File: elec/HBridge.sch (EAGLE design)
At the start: 22 parts, among them IC1 TL082P, IC2 TL082P, IC3 TL082P, T1 QSD124N

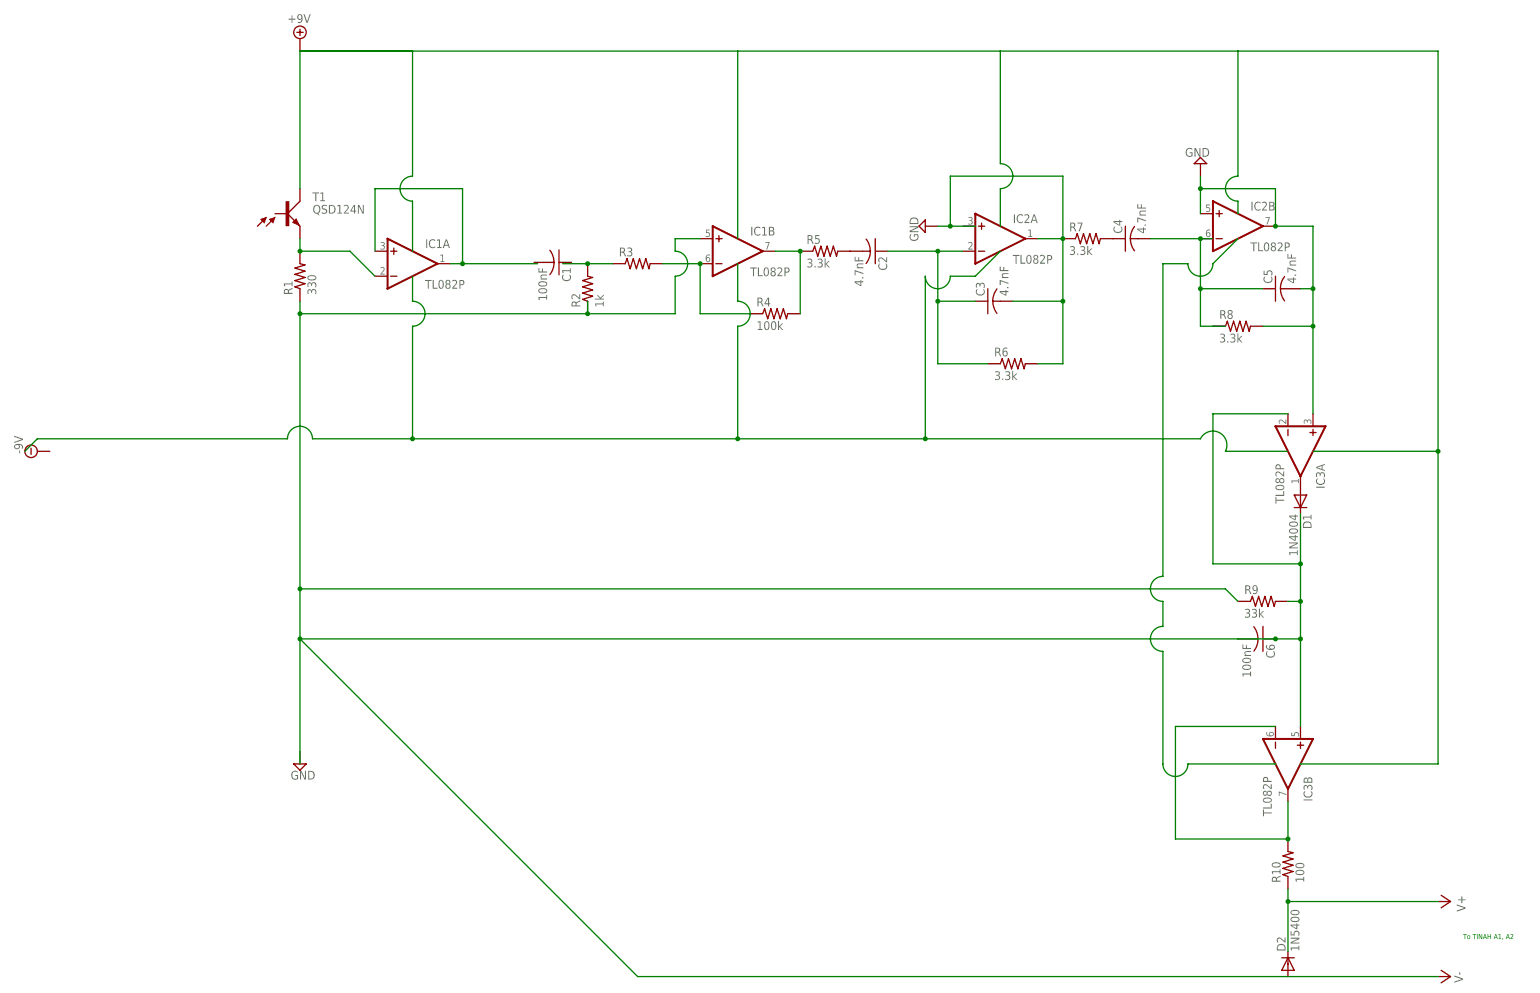
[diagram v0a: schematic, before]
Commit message: Hbridge and IR Detector circuits modified version June 13
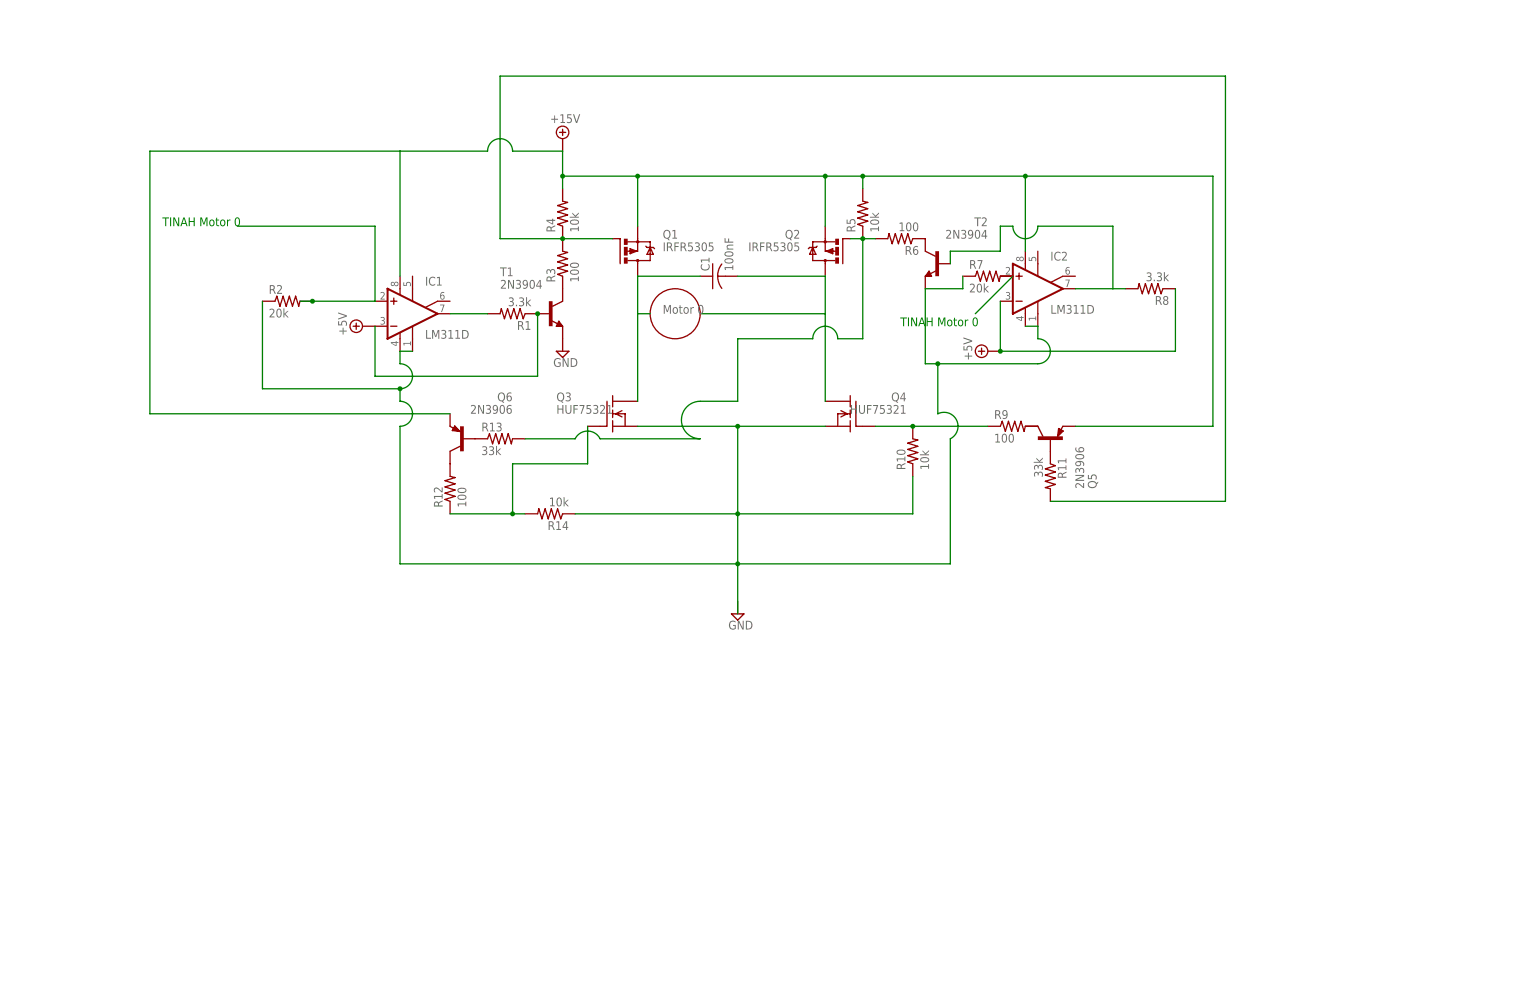
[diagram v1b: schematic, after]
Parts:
- removed C2: 4.7nF, resistor:C-US025-025X050
- removed C3: 4.7nF, resistor:C-US050-055X075
- removed C4: 4.7nF, resistor:C-US225-087X268
- removed C5: 4.7nF, resistor:C-US050-045X075
- removed C6: 100nF, resistor:C-US025-060X050
- removed D1: 1N4004, diode:1N4004
- removed D2: 1N5400, diode:1N5400
- removed IC3: TL082P, linear:TL082P
- added Q1, Q2: IRFR5305, transistor-power:IRFR5305
- added Q3, Q4: HUF75321, transistor-fet:FDS5680
- added Q5, Q6: 2N3906, transistor-pnp:2N3906
- added R11, R13: 33k, resistor:R-US_0204/2V
- added R12: 100, resistor:R-US_0204/2V
- added R14: 10k, resistor:R-US_0204/2V
- added T2: 2N3904, transistor:2N3904
- IC1, IC2: value TL082P -> LM311D; device linear:TL082P -> linear:LM311D
- R1: value 330 -> 3.3k; device resistor:R-US_0204/5 -> resistor:R-US_0204/2V
- R10: value 100 -> 10k; device resistor:R-US_0414/5V -> resistor:R-US_0204/2V
- R2: value 1k -> 20k; device resistor:R-US_0204/5 -> resistor:R-US_0204/2V
- R3: value (none) -> 100; device resistor:R-US_0207/5V -> resistor:R-US_0204/2V
- R4: value 100k -> 10k; device resistor:R-US_01005 -> resistor:R-US_0204/2V
- R5: value 3.3k -> 10k; device resistor:R-US_01005 -> resistor:R-US_0204/2V
- R6: value 3.3k -> 100; device resistor:R-US_0207/5V -> resistor:R-US_0204/2V
- R7: value 3.3k -> 20k; device resistor:R-US_0207/5V -> resistor:R-US_0204/2V
- R8: device resistor:R-US_0309/12 -> resistor:R-US_0204/2V
- R9: value 33k -> 100; device resistor:R-US_0207/5V -> resistor:R-US_0204/2V
- T1: value QSD124N -> 2N3904; device opto-trans-siemens:BP103 -> transistor:2N3904
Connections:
- removed net V+: D2.C, R10.1
- removed net V-: C6.1, C6.2, D1.C, D2.A, IC1B.+IN, IC3A.-IN, IC3B.+IN, R1.1, R2.1, R9.1, R9.2
- new net +5V: IC1.-IN, IC2.-IN, R1.1, R8.1, T1.B
- new net N$10: R7.2
- new net N$11: IC2.OUT, R8.2, T2.B
- new net N$15: Q6.B, R13.1
- new net N$16: Q3.G, R12.1, R14.2
- new net N$3: R3.1, T1.C
- net +15V: now also IC1.V+, IC2.V+, Q1.S, Q2.S, Q5.E, Q6.E, R4.2, R5.2; no longer T1.C
- net GND: now also T1.E; no longer C3.2, C5.2, IC2A.OUT, IC2B.+IN, IC2B.OUT, IC3A.+IN, R6.2, R7.1, R8.2
- net N$1: now also IC1.OUT; no longer IC1A.-IN, T1.E
- net N$12: now also Q1.G, R11.2, R3.2, R4.1; no longer IC3B.-IN, IC3B.OUT, R10.2
- net N$13: now also Q5.B, R11.1; no longer C4.1, R7.2
- net N$14: now also Q6.C, R12.2; no longer C4.2, C5.1, IC2B.-IN, R8.1
- net N$2: now also IC1.+IN, R2.2; no longer IC1A.+IN, IC1A.OUT
- net N$4: now also Q2.G, R13.2, R5.1, R6.2; no longer IC1B.-IN, R3.2, R4.1
- net N$5: now also IC1.GND, IC1.V-, IC2.GND, IC2.V-, Q3.S, Q4.S, R10.1, R14.1, R2.1, R7.1, T2.E; no longer IC1B.OUT, R4.2, R5.1
- net N$6: now also C1.2, Q2.D, Q4.D; no longer R2.2, R3.1
- net N$7: now also C1.1, Q1.D, Q3.D; no longer C2.1, C3.1, IC2A.-IN, R6.1
- net N$8: now also R6.1, T2.C; no longer C2.2, R5.2
- net N$9: now also Q4.G, R10.2, R9.1; no longer D1.A, IC3A.OUT
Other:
- note added: "Motor 0"
- note added: "TINAH Motor 0"
- note removed: "To TINAH A1, A2"
- moved on the sheet: C1, R1, R10, R2, R3, R4, R5, R6, R7, R8, R9

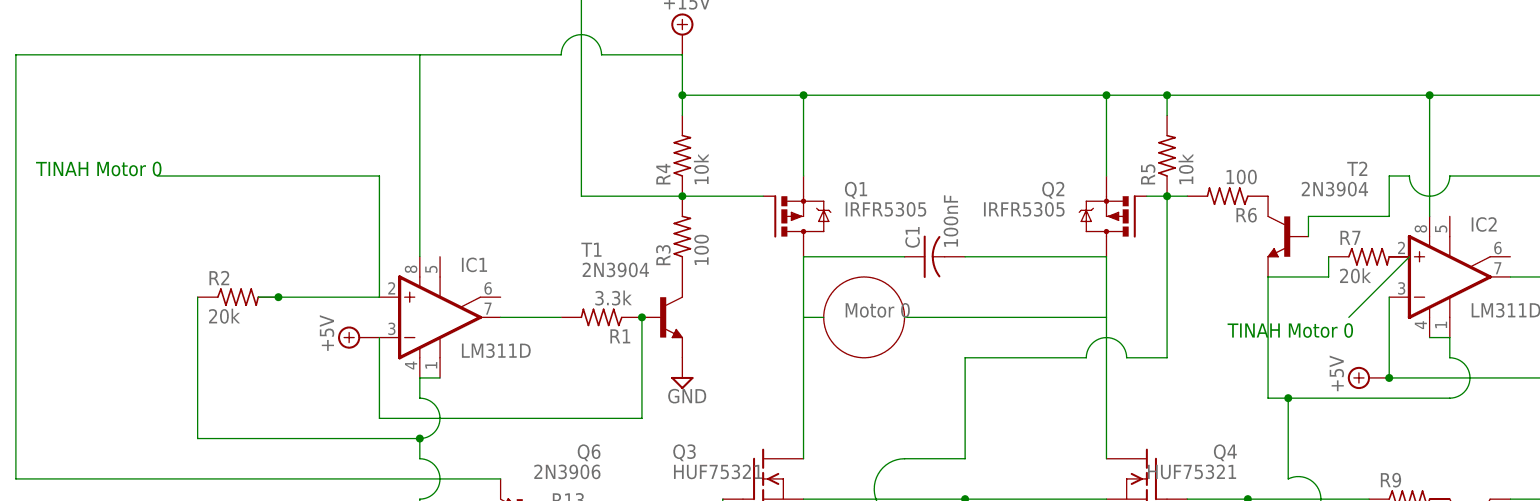
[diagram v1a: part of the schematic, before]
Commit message: Updated H bridge
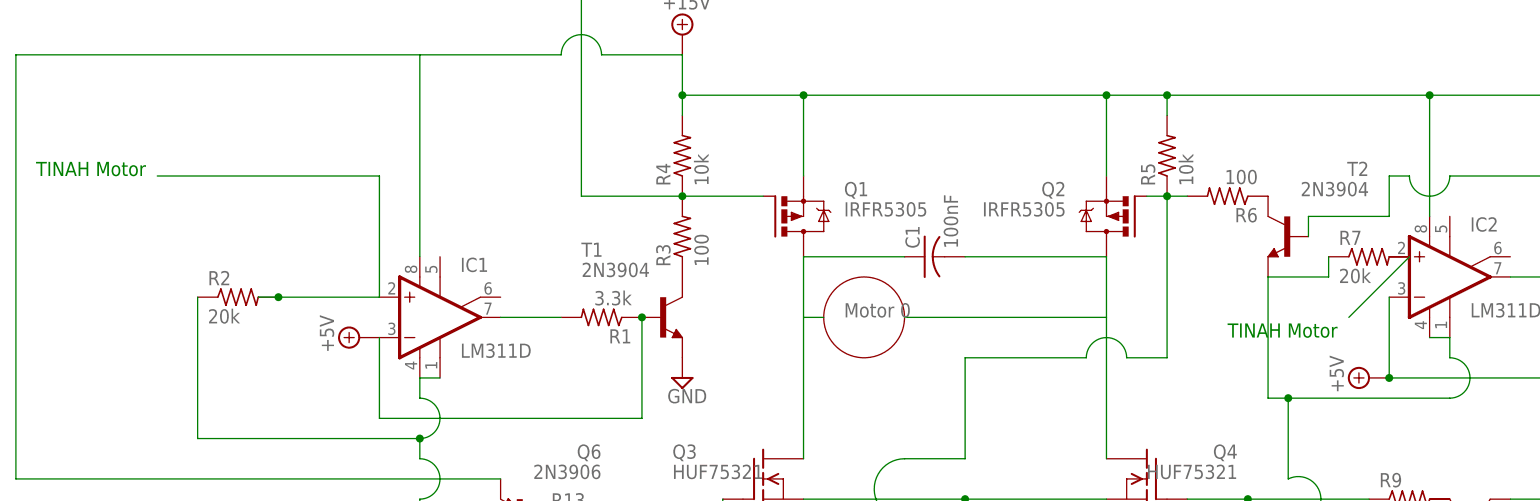
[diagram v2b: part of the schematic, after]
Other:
- note added: "TINAH Motor"
- note removed: "TINAH Motor 0"
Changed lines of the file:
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@@
 <sheet>
 <plain>
-<text x="-43.18" y="71.12" size="1.778" layer="91">TINAH Motor 0</text>
+<text x="-43.18" y="71.12" size="1.778" layer="91">TINAH Motor </text>
 <circle x="60.96" y="53.34" radius="5.08" width="0.1524" layer="94"/>
 <text x="58.42" y="53.34" size="1.778" layer="95">Motor 0</text>
-<text x="106.68" y="50.8" size="1.778" layer="91">TINAH Motor 0</text>
+<text x="106.68" y="50.8" size="1.778" layer="91">TINAH Motor </text>
 </plain>
 <instances>

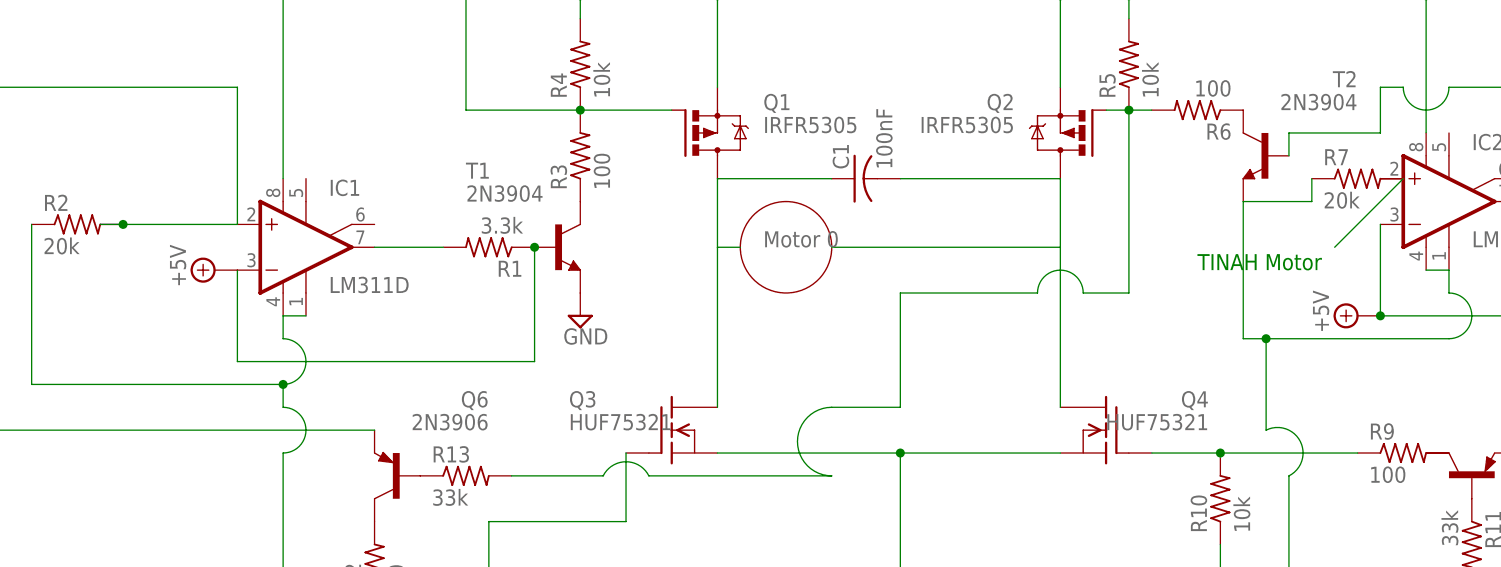
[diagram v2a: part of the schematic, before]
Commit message: Voltage regulators added if necessary
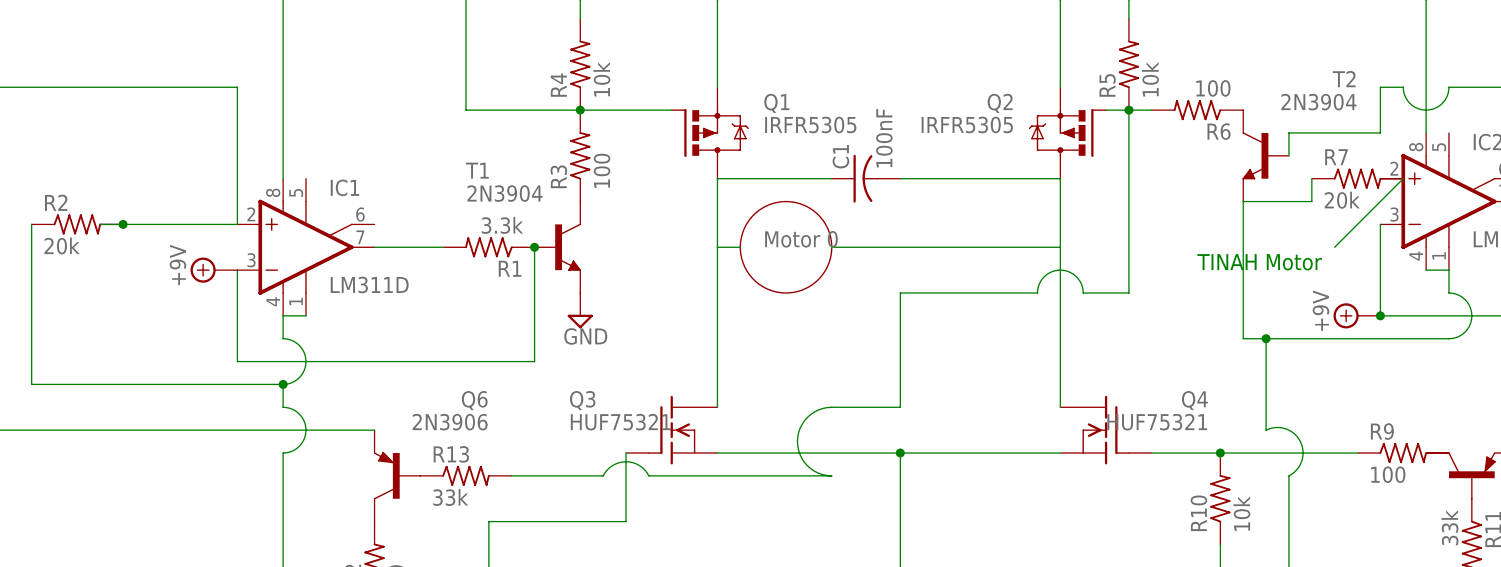
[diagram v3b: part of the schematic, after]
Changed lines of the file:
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@@
 <parts>
 <part name="IC1" library="linear" deviceset="LM311" device="D"/>
-<part name="SUPPLY3" library="supply2" deviceset="+5V" device=""/>
+<part name="SUPPLY3" library="supply2" deviceset="+5V" device="" value="+9V"/>
 <part name="R1" library="resistor" deviceset="R-US_" device="0204/2V" value="3.3k"/>
 <part name="R2" library="resistor" deviceset="R-US_" device="0204/2V" value="20k"/>
@@
 <part name="R7" library="resistor" deviceset="R-US_" device="0204/2V" value="20k"/>
 <part name="R8" library="resistor" deviceset="R-US_" device="0204/2V" value="3.3k"/>
-<part name="SUPPLY5" library="supply2" deviceset="+5V" device=""/>
+<part name="SUPPLY5" library="supply2" deviceset="+5V" device="" value="+9V"/>
 <part name="R9" library="resistor" deviceset="R-US_" device="0204/2V" value="100"/>
 <part name="Q5" library="transistor-pnp" deviceset="2N3906" device=""/>
